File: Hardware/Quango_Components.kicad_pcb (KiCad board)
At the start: 2 copper layers, 80.7 x 100 mm, 167 parts, among them J1 Conn_01x12_Male, J2 Conn_01x12_Male, J3 Conn_01x12_Male, J4 Conn_01x12_Male, J5 SWD_Header, J6 Eurorack_10_pin_power, Q1 MMBT3904, U1 LM1117-3.3, U10 TL074, U11 TL074, U12 TL074, U13 TL074, U14 TL074, U2 STM32G473V, U3 LM1117-5.0, U4 PS508, U5 MCP6002, U6 AS3364, U7 AS3364, U8 AD5676, U9 MCP48CMB21, Y1 8MHz 20pF

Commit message: Started laying out control board
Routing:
- added copper zone on In1.Cu, net GND
- added copper zone on In2.Cu, net GND
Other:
- copper layers 2 -> 4
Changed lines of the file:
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@@
 (kicad_pcb (version 20211014) (generator pcbnew)
   (general
-    (thickness 1.6)
+    (thickness 4.69)
   )
   (paper "A4")
   (layers
     (0 "F.Cu" signal)
+    (1 "In1.Cu" signal)
+    (2 "In2.Cu" signal)
     (31 "B.Cu" signal)
     (34 "B.Paste" user)
@@
   (setup
     (stackup
-      (layer "F.SilkS" (type "Top Silk Screen"))
+      (layer "F.SilkS" (type "Top Silk Screen") (color "White"))
       (layer "F.Paste" (type "Top Solder Paste"))
-      (layer "F.Mask" (type "Top Solder Mask") (thickness 0.01))
+      (layer "F.Mask" (type "Top Solder Mask") (color "Green") (thickness 0.01))
       (layer "F.Cu" (type "copper") (thickness 0.035))
       (layer "dielectric 1" (type "core") (thickness 1.51) (material "FR4") (epsilon_r 4.5) (loss_tangent 0.02))
+      (layer "In1.Cu" (type "copper") (thickness 0.035))
+      (layer "dielectric 2" (type "prepreg") (thickness 1.51) (material "FR4") (epsilon_r 4.5) (loss_tangent 0.02))
+      (layer "In2.Cu" (type "copper") (thickness 0.035))
+      (layer "dielectric 3" (type "core") (thickness 1.51) (material "FR4") (epsilon_r 4.5) (loss_tangent 0.02))
       (layer "B.Cu" (type "copper") (thickness 0.035))
-      (layer "B.Mask" (type "Bottom Solder Mask") (thickness 0.01))
+      (layer "B.Mask" (type "Bottom Solder Mask") (color "Green") (thickness 0.01))
       (layer "B.Paste" (type "Bottom Solder Paste"))
-      (layer "B.SilkS" (type "Bottom Silk Screen"))
+      (layer "B.SilkS" (type "Bottom Silk Screen") (color "White"))
       (copper_finish "None")
       (dielectric_constraints no)
@@
   (segment (start 109.8625 119.825) (end 112.3 119.825) (width 0.25) (layer "F.Cu") (net 187))
   (segment (start 112.375 103.4) (end 109.05 103.4) (width 0.25) (layer "F.Cu") (net 188))
-  (zone (net 1) (net_name "GND") (layers F&B.Cu) (hatch edge 0.508)
+  (zone (net 1) (net_name "GND") (layers "F.Cu" "In1.Cu" "In2.Cu" "B.Cu") (hatch edge 0.508)
     (connect_pads (clearance 0.508))
     (min_thickness 0.254) (filled_areas_thickness no)

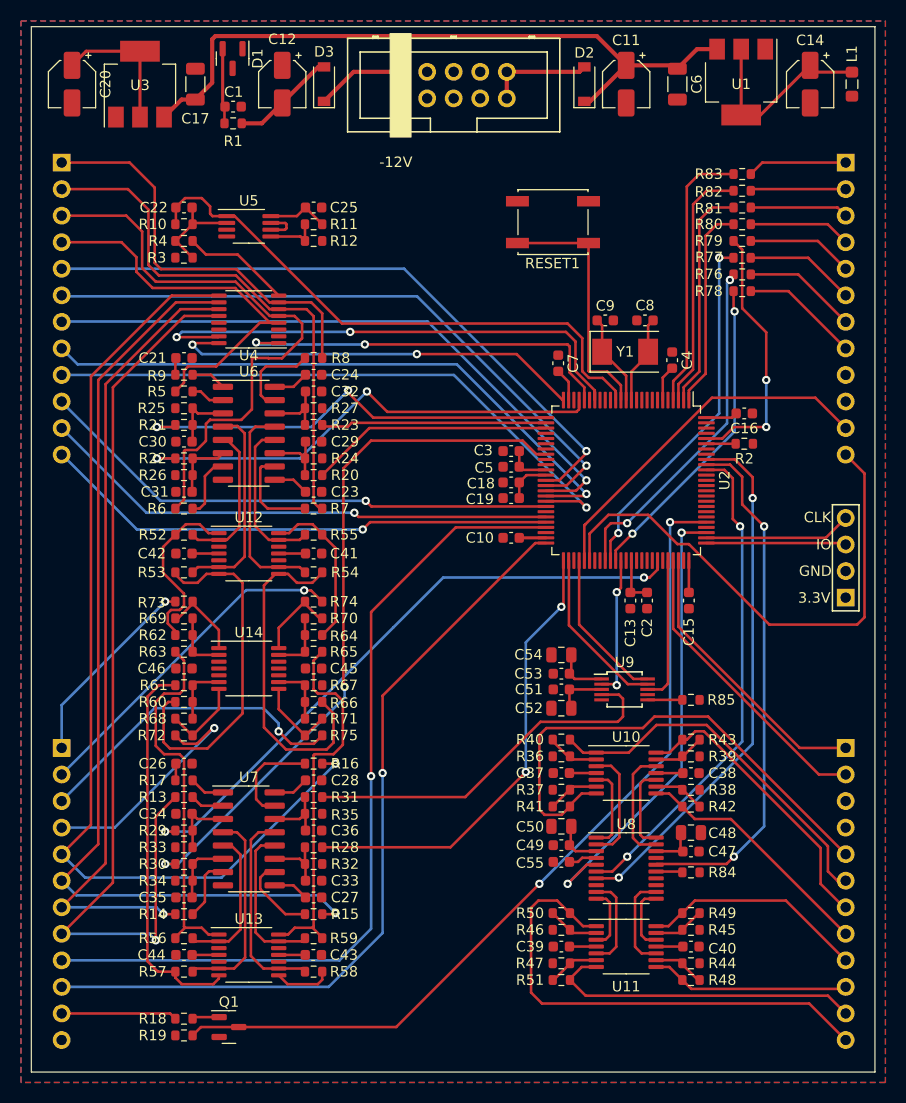
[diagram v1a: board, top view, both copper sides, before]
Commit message: Reduced module size to 14HP; updated to Amphenol USB C
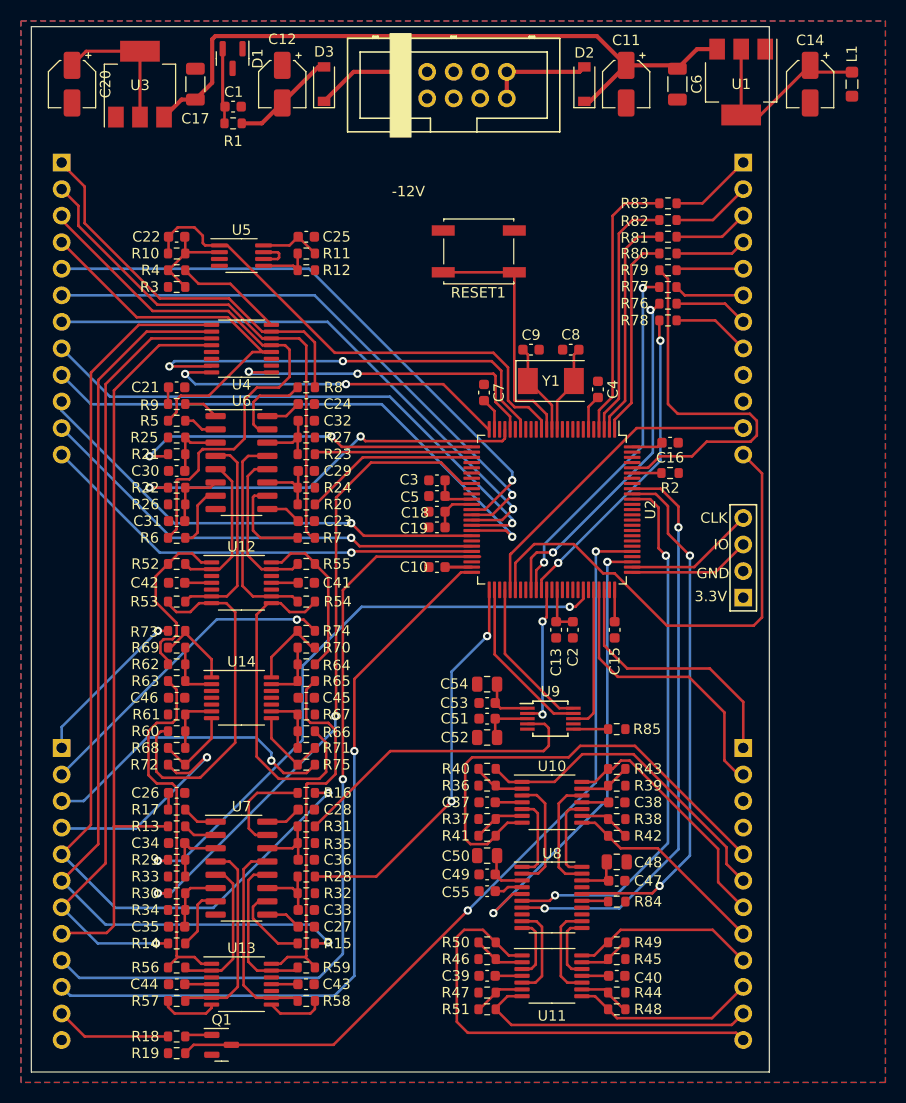
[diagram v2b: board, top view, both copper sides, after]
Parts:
- moved J3 9.80 mm to (118.2, 52.0)
- moved J4 9.80 mm to (118.2, 108.0)
- moved J5 9.80 mm to (118.2, 93.6)
- moved C40 7.63 mm to (106.1, 129.8)
- moved C48 7.63 mm to (106.1, 118.9)
- moved R38 7.63 mm to (106.1, 114.8)
- moved R44 7.63 mm to (106.1, 131.4)
- moved R48 7.63 mm to (106.1, 133.0)
- moved Y1 7.63 mm to (99.8, 72.9)
- moved C13 7.63 mm to (100.3, 96.7)
- moved C38 7.63 mm to (106.1, 113.2)
- moved C4 7.63 mm to (104.3, 73.7)
- moved C47 7.63 mm to (106.1, 120.7)
- moved R39 7.63 mm to (106.1, 111.6)
- moved R42 7.63 mm to (106.1, 116.4)
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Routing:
- net /OpAmps/AudioB1_Out: track 37.1 -> 5.53 mm
- net /AudioB1_In: track 91.0 -> 72.7 mm, vias 1 -> 0
- net /EnvA4_LED: track 25.3 -> 36.9 mm, vias 2 -> 0
- net /EnvA1_DAC: track 41.7 -> 33.9 mm
- net /EnvA2_DAC: track 46.6 -> 39.0 mm
- net /MIDI_UART: track 82.4 -> 75.6 mm
- net /EnvA4_DAC: track 21.6 -> 15.1 mm
- net /Env2_Release: track 49.6 -> 43.2 mm
- net /MultiplexerA0: track 38.1 -> 31.7 mm
- net /EnvB4_DAC: track 35.9 -> 29.5 mm
- net /EnvA3_DAC: track 23.3 -> 16.9 mm
- net /EnvB3_DAC: track 44.2 -> 37.8 mm
- net /Audio_In_Multiplexed: track 54.9 -> 48.5 mm
- net /MultiplexerA1: track 40.3 -> 33.9 mm
- net /MultiplexerA2: track 50.0 -> 43.6 mm
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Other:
- board size 80.7 x 100 mm -> 70.6 x 100 mm

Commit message: Added individual audio channel breakout
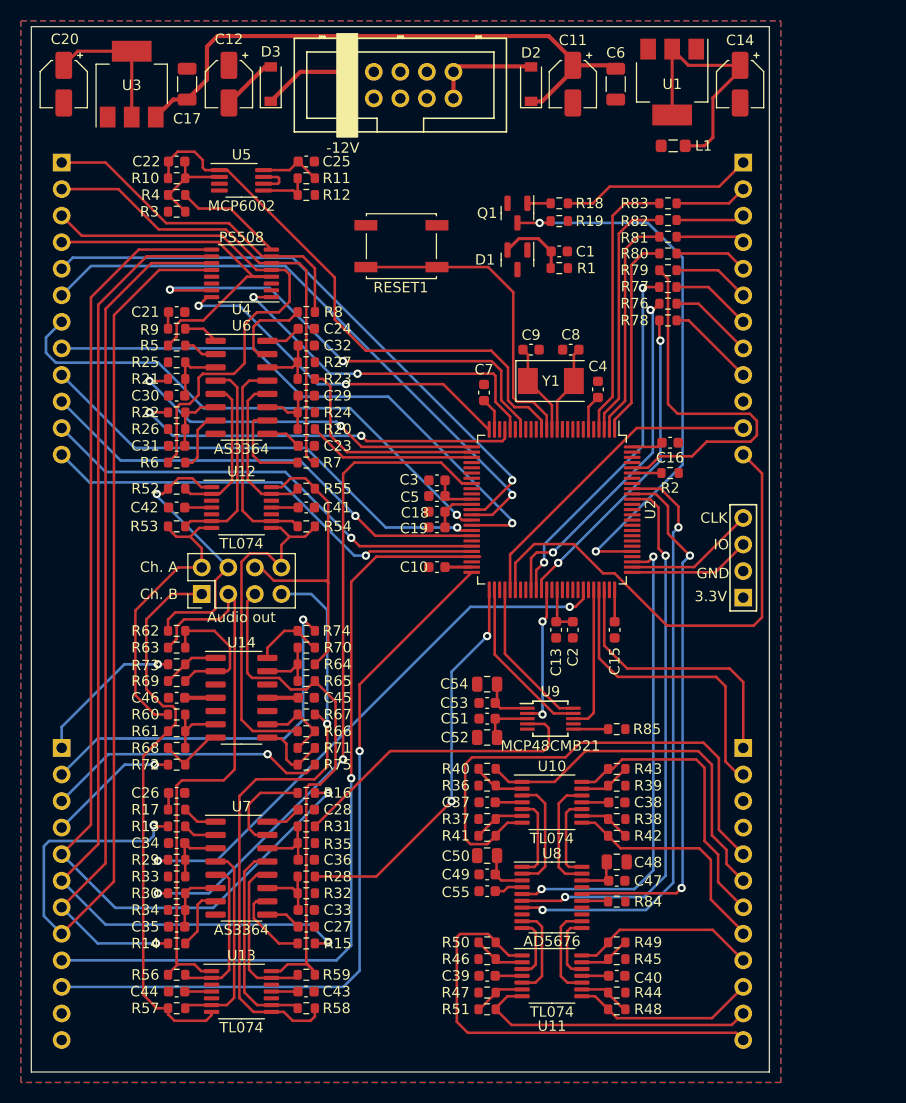
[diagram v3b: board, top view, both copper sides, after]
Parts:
- added J7: Audio_Breakout, Connector_PinHeader_2.54mm:PinHeader_2x04_P2.54mm_Vertical, F.Cu at (66.4, 93.3)
- U14: footprint Package_SO:TSSOP-14_4.4x5mm_P0.65mm -> Package_SO:SOIC-14_3.9x8.7mm_P1.27mm
- moved R18 87.7 mm to (100.6, 55.9), turned to 180 degrees
- moved R19 87.6 mm to (100.6, 57.6), turned to 0 degrees
- moved Q1 84.4 mm to (96.6, 56.8), turned to -90 degrees
- moved C1 34.1 mm to (100.6, 60.5)
- moved R1 34.1 mm to (100.6, 62.1)
- moved D1 33.4 mm to (96.6, 61.3)
- moved L1 18.1 mm to (111.5, 50.4), turned to 180 degrees
- moved RESET1 7.42 mm to (85.5, 60.0)
- moved C21 7.20 mm to (64.0, 66.3)
- moved C22 7.20 mm to (64.0, 51.9)
- moved C23 7.20 mm to (76.4, 79.1)
- moved C25 7.20 mm to (76.4, 51.9)
- moved C29 7.20 mm to (76.4, 74.3)
- moved C30 7.20 mm to (64.0, 74.3)
- moved C31 7.20 mm to (64.0, 79.1)
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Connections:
- J2 pad 11: /MIDI_IN -> +3.3VA
- J3 pad 1: /EnvB4_LED_Out -> /MIDI_IN
- J3 pad 2: /EnvB3_LED_Out -> /EnvB4_LED_Out
- J3 pad 3: /EnvB2_LED_Out -> /EnvB3_LED_Out
- J3 pad 4: /EnvB1_LED_Out -> /EnvB2_LED_Out
- J3 pad 5: /EnvA4_LED_Out -> /EnvB1_LED_Out
- J3 pad 6: /EnvA2_LED_Out -> /EnvA4_LED_Out
- J3 pad 7: /EnvA1_LED_Out -> /EnvA2_LED_Out
- J3 pad 8: /EnvA3_LED_Out -> /EnvA1_LED_Out
- J3 pad 9: +3.3VA -> /EnvA3_LED_Out
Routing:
- net /OpAmps/AudioB4_Out: track 5.47 -> 59.5 mm, vias 0 -> 1
- net /OpAmps/AudioB1_Out: track 5.53 -> 53.6 mm
- net /MIDI_UART: track 75.6 -> 53.3 mm
- net /AudioB1_In: track 72.7 -> 94.8 mm, vias 0 -> 1
- net /OpAmps/AudioB2_Out: track 35.7 -> 55.7 mm
- net /OpAmps/AudioA3_Out: track 15.6 -> 30.5 mm
- net /OpAmps/AudioB3_Out: track 36.0 -> 50.7 mm
- net /OpAmps/AudioA2_Out: track 17.3 -> 26.6 mm, vias 0 -> 1
- net /Audio1_Out: track 21.4 -> 12.7 mm
- net /Env2_Attack: track 53.8 -> 45.4 mm
- net Net-(R62-Pad1): track 6.04 -> 13.4 mm
- net /MIDI_IN: track 11.1 -> 18.4 mm
- net /AudioB3_In: track 91.4 -> 98.6 mm
- net /AudioB4_In: track 94.1 -> 101.3 mm
- net /AudioB2_In: track 75.3 -> 82.5 mm
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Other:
- board text added: "Audio out"
- board text added: "Ch. A"
- board text added: "Ch. B"

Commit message: Routing Power traces
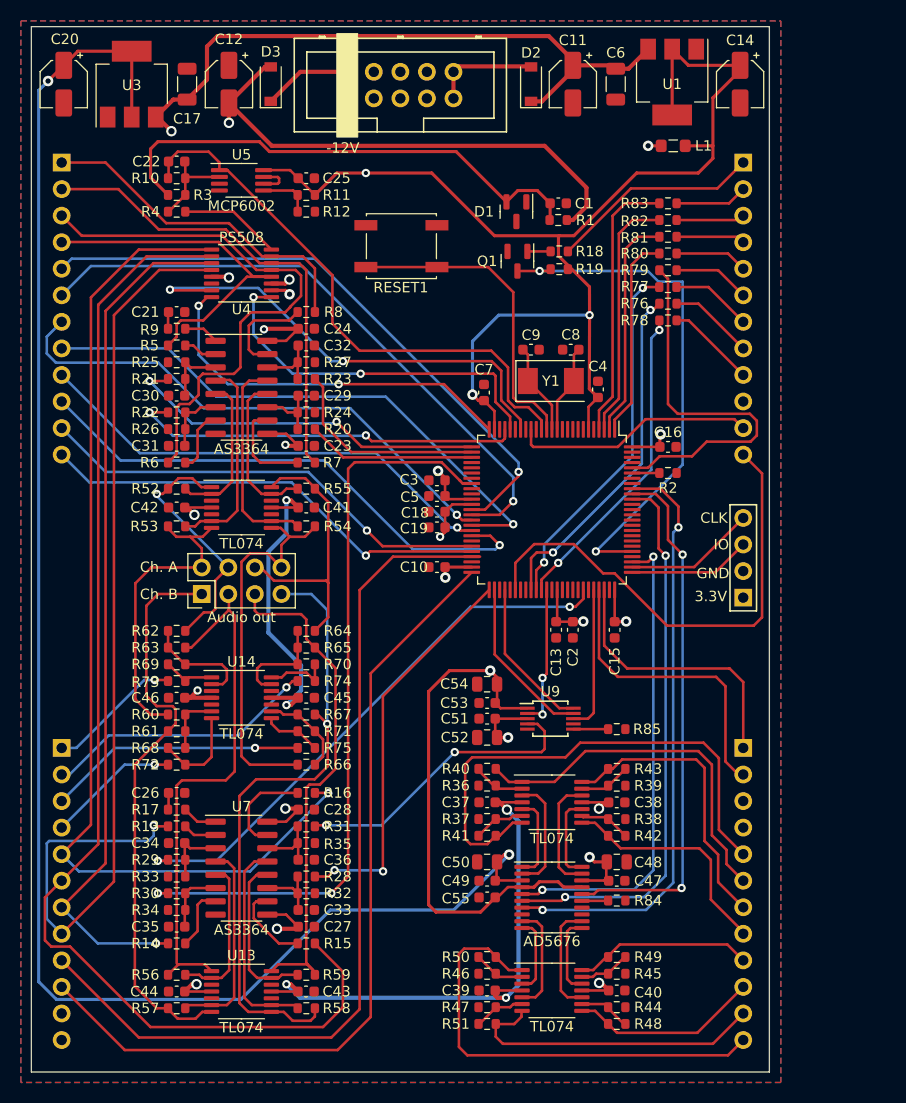
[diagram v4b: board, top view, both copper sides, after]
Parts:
- U14: footprint Package_SO:SOIC-14_3.9x8.7mm_P1.27mm -> Package_SO:TSSOP-14_4.4x5mm_P0.65mm
- moved R74 4.80 mm to (76.4, 101.6), turned to 0 degrees
- moved C1 4.60 mm to (100.5, 55.9)
- moved R1 4.60 mm to (100.5, 57.5)
- moved D1 4.60 mm to (96.5, 56.7)
- moved Q1 4.60 mm to (96.6, 61.4)
- moved R18 4.60 mm to (100.6, 60.5)
- moved R19 4.60 mm to (100.6, 62.2)
- moved R64 3.20 mm to (76.4, 96.8)
- moved R65 3.20 mm to (76.4, 98.4)
- moved R66 3.20 mm to (76.4, 109.6)
- moved C25 1.60 mm to (76.4, 53.5)
- moved R11 1.60 mm to (76.4, 55.1)
- moved R12 1.60 mm to (76.4, 56.7)
- moved R3 1.60 mm to (64.0, 55.1)
- moved R4 1.60 mm to (64.0, 56.7)
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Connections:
- U2 pad 17: unconnected-(U2-Pad17) -> /ChannelA_Level
- U2 pad 55: /ChannelA_Level -> unconnected-(U2-Pad55)
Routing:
- net -12V: track 26.3 -> 245.1 mm, vias 0 -> 9
- net +3.3V: track 58.1 -> 272.2 mm, vias 0 -> 9
- net +3.3VA: track 13.2 -> 199.6 mm, vias 0 -> 4
- net +5V: track 22.3 -> 173.3 mm, vias 0 -> 3
- net +12V: track 77.4 -> 226.5 mm, vias 0 -> 9
- net /-5V_REF: track 6.68 -> 48.6 mm
- net /AudioB3_In: track 98.6 -> 115.6 mm, vias 1 -> 0
- net /Audio3_Out: track 36.4 -> 26.3 mm
- net /Calib_Btn1: track 76.4 -> 85.6 mm, vias 1 -> 0
- net /Calib_Btn2: track 71.7 -> 79.9 mm, vias 1 -> 0
- net /ChannelA_Level: track 30.7 -> 23.3 mm
- net /EnvB2_DAC: track 64.9 -> 71.8 mm
- net /Env2_Decay: track 44.5 -> 51.0 mm
- net /OpAmps/AudioB2_Out: track 55.7 -> 50.8 mm
- net Net-(R64-Pad1): track 6.37 -> 9.87 mm
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
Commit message: Added Test Points
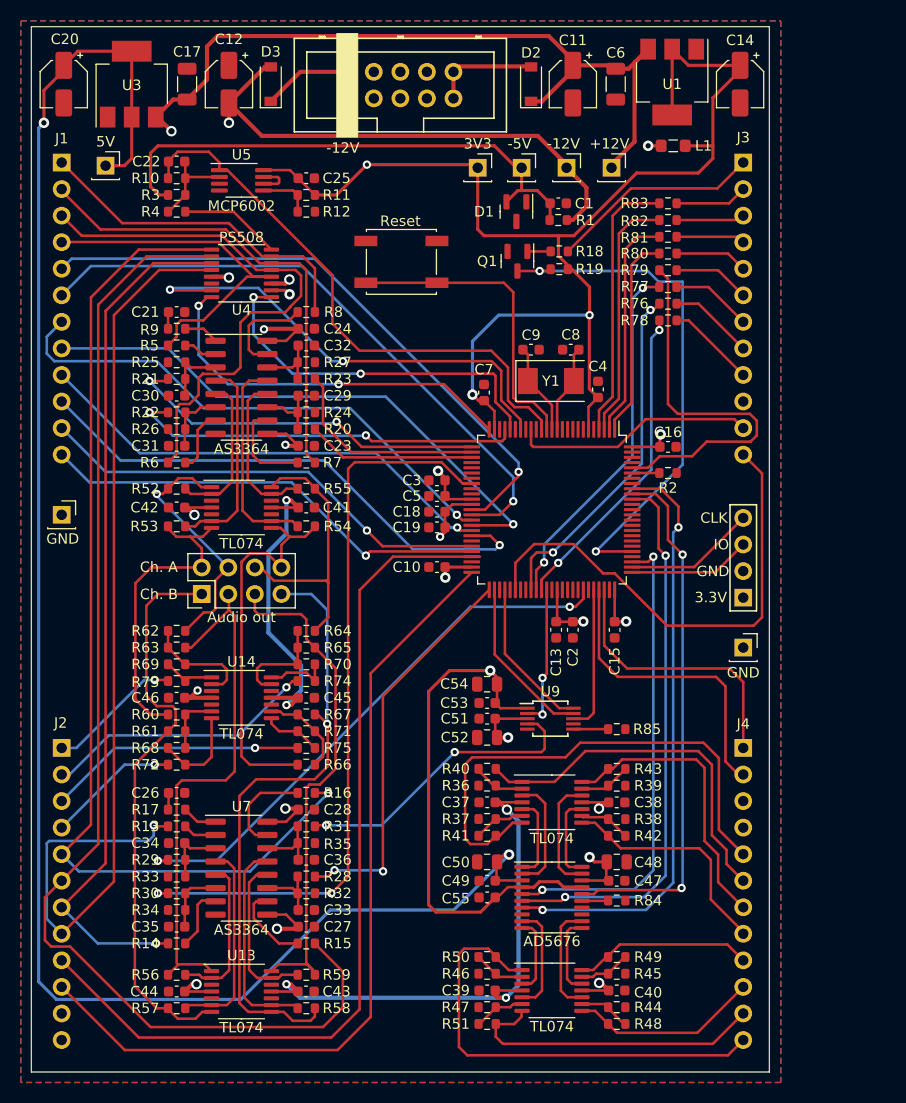
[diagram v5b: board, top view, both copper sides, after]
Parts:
- added TP1: TestPoint, Connector_PinSocket_2.54mm:PinSocket_1x01_P2.54mm_Vertical, F.Cu at (105.6, 52.5)
- added TP2: TestPoint, Connector_PinSocket_2.54mm:PinSocket_1x01_P2.54mm_Vertical, F.Cu at (101.3, 52.5)
- added TP3: TestPoint, Connector_PinSocket_2.54mm:PinSocket_1x01_P2.54mm_Vertical, F.Cu at (57.2, 52.3)
- added TP4: TestPoint, Connector_PinSocket_2.54mm:PinSocket_1x01_P2.54mm_Vertical, F.Cu at (97.0, 52.5)
- added TP5: TestPoint, Connector_PinSocket_2.54mm:PinSocket_1x01_P2.54mm_Vertical, F.Cu at (92.8, 52.5)
- added TP6: TestPoint, Connector_PinSocket_2.54mm:PinSocket_1x01_P2.54mm_Vertical, F.Cu at (53.0, 85.7)
- added TP7: TestPoint, Connector_PinSocket_2.54mm:PinSocket_1x01_P2.54mm_Vertical, F.Cu at (118.2, 98.4)
- moved RESET1 1.50 mm to (85.5, 61.5)
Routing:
- net +12V: track 226.5 -> 239.3 mm
- net +5V: track 173.3 -> 180.6 mm
- net +3.3VA: track 199.6 -> 205.2 mm
- net +3.3V: track 272.2 -> 277.1 mm
- net /-5V_REF: track 48.6 -> 50.8 mm
- net /RESET: track 30.4 -> 29.8 mm
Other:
- board text added: "+12V"
- board text added: "-12V"
- board text added: "-5V"
- board text added: "3V3"
- board text added: "5V"
- board text added: "GND"
- board text added: "J1"
- board text added: "J2"
- board text added: "J3"
- board text added: "J4"
- board text added: "Reset"

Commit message: Preparing panel and control board for routing
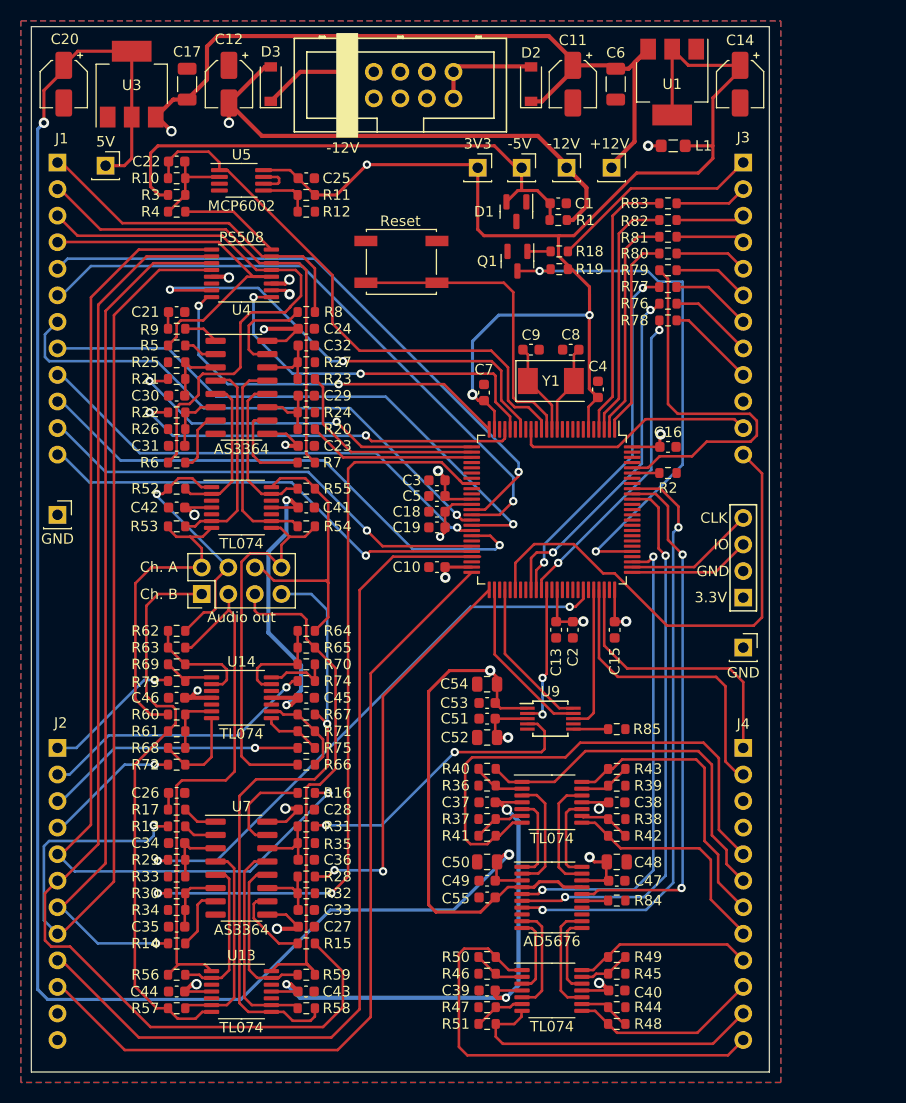
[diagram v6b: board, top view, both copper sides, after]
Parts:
- moved J1 0.40 mm to (52.6, 52.0)
- moved J2 0.40 mm to (52.6, 108.0)
- moved TP6 0.40 mm to (52.6, 85.7)
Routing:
- net /AudioB2_In: track 82.4 -> 83.2 mm
- net /AudioB4_In: track 98.4 -> 99.2 mm
- net +5V: track 180.6 -> 181.2 mm
